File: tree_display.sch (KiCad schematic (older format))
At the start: 8 parts

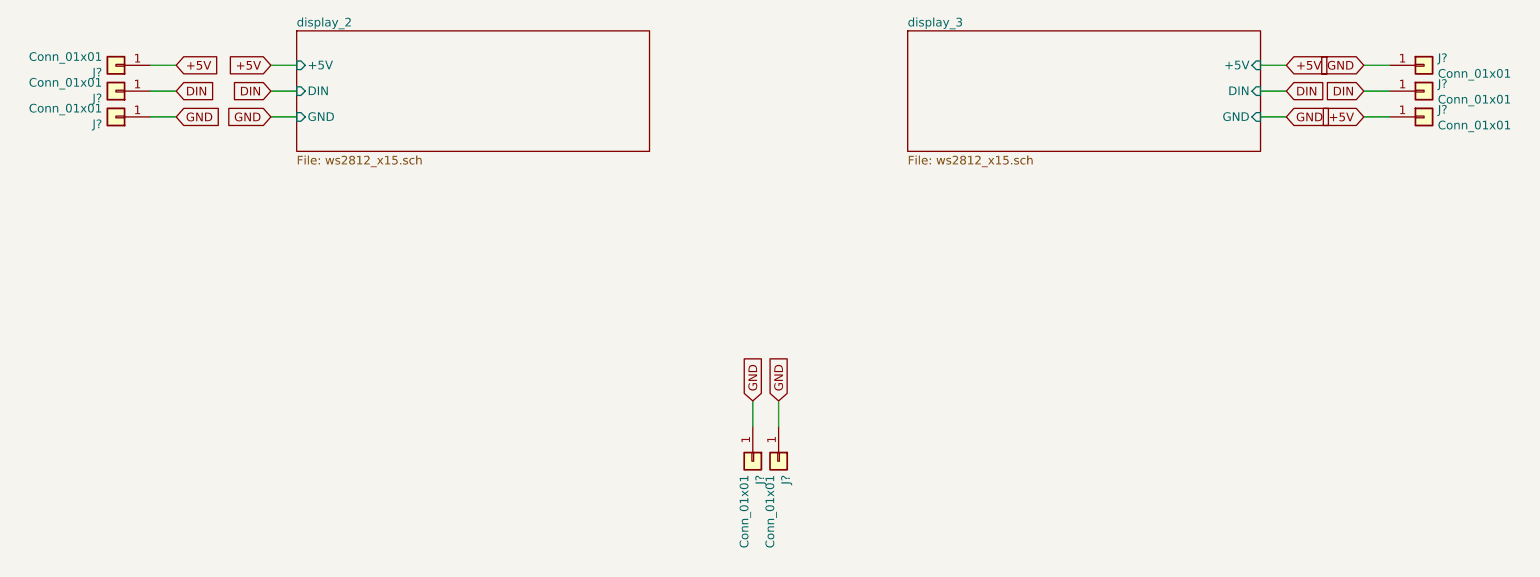
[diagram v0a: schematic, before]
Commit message: Update with changes to use attiny13a only
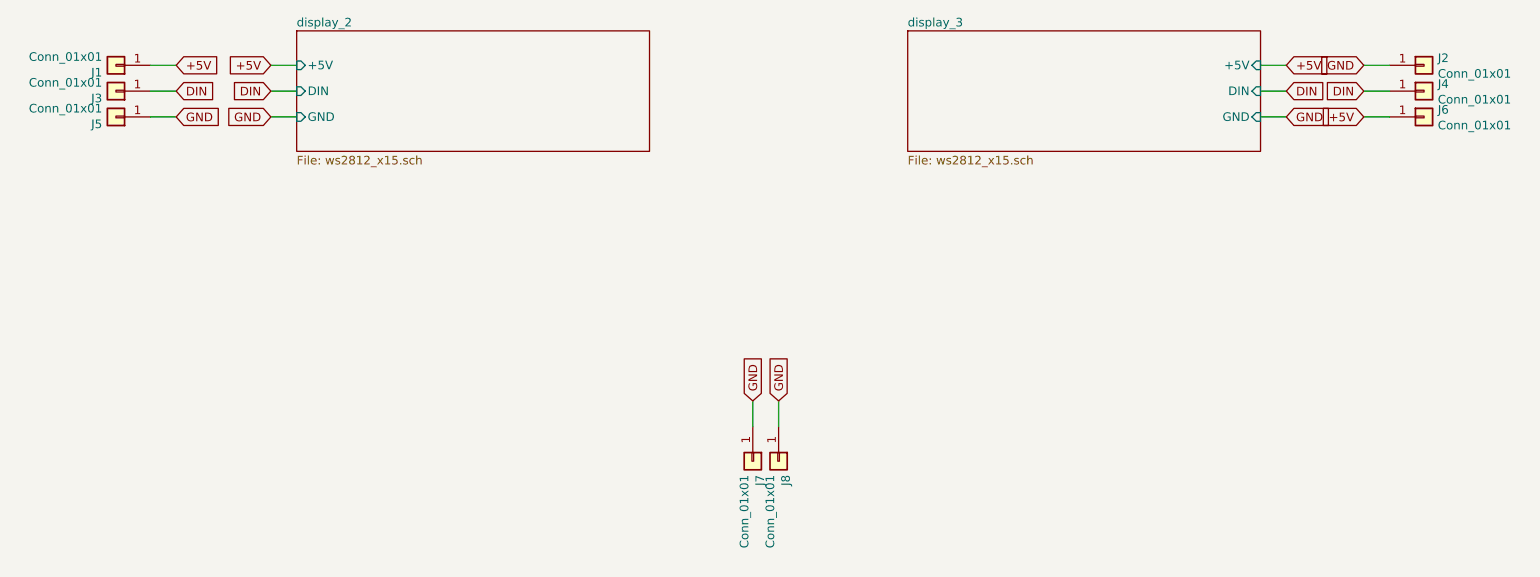
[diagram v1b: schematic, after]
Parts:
- gave numbers to parts that had none: 8
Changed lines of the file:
@@
 $EndDescr
 $Comp
-L Connector_Generic:Conn_01x01 J?
+L Connector_Generic:Conn_01x01 J6
 U 1 1 5FC428C8
 P 9750 3550
-F 0 "J?" H 9830 3592 50  0000 L CNN
+F 0 "J6" H 9830 3592 50  0000 L CNN
 F 1 "Conn_01x01" H 9830 3501 50  0000 L CNN
 F 2 "TestPoint:TestPoint_Pad_2.0x2.0mm" H 9750 3550 50  0001 C CNN
@@
 	9550 3550 9400 3550
 $Comp
-L Connector_Generic:Conn_01x01 J?
+L Connector_Generic:Conn_01x01 J4
 U 1 1 5FC43693
 P 9750 3400
-F 0 "J?" H 9830 3442 50  0000 L CNN
+F 0 "J4" H 9830 3442 50  0000 L CNN
 F 1 "Conn_01x01" H 9830 3351 50  0000 L CNN
 F 2 "TestPoint:TestPoint_Pad_2.0x2.0mm" H 9750 3400 50  0001 C CNN
@@
 	9550 3400 9400 3400
 $Comp
-L Connector_Generic:Conn_01x01 J?
+L Connector_Generic:Conn_01x01 J2
 U 1 1 5FC43C3D
 P 9750 3250
-F 0 "J?" H 9830 3292 50  0000 L CNN
+F 0 "J2" H 9830 3292 50  0000 L CNN
 F 1 "Conn_01x01" H 9830 3201 50  0000 L CNN
 F 2 "TestPoint:TestPoint_Pad_2.0x2.0mm" H 9750 3250 50  0001 C CNN
@@
 	9550 3250 9400 3250
 $Comp
-L Connector_Generic:Conn_01x01 J?
+L Connector_Generic:Conn_01x01 J1
 U 1 1 5FC48F56
 P 2150 3250
-F 0 "J?" H 2230 3292 50  0000 L CNN
+F 0 "J1" H 2230 3292 50  0000 L CNN
 F 1 "Conn_01x01" H 2230 3201 50  0000 L CNN
 F 2 "TestPoint:TestPoint_Pad_2.0x2.0mm" H 2150 3250 50  0001 C CNN
@@
 	2350 3250 2500 3250
 $Comp
-L Connector_Generic:Conn_01x01 J?
+L Connector_Generic:Conn_01x01 J3
 U 1 1 5FC48F5E
 P 2150 3400
-F 0 "J?" H 2230 3442 50  0000 L CNN
+F 0 "J3" H 2230 3442 50  0000 L CNN
 F 1 "Conn_01x01" H 2230 3351 50  0000 L CNN
 F 2 "TestPoint:TestPoint_Pad_2.0x2.0mm" H 2150 3400 50  0001 C CNN
@@
 	2350 3400 2500 3400
 $Comp
-L Connector_Generic:Conn_01x01 J?
+L Connector_Generic:Conn_01x01 J5
 U 1 1 5FC48F66
 P 2150 3550
-F 0 "J?" H 2230 3592 50  0000 L CNN
+F 0 "J5" H 2230 3592 50  0000 L CNN
 F 1 "Conn_01x01" H 2230 3501 50  0000 L CNN
 F 2 "TestPoint:TestPoint_Pad_2.0x2.0mm" H 2150 3550 50  0001 C CNN
@@
 GND
 $Comp
-L Connector_Generic:Conn_01x01 J?
+L Connector_Generic:Conn_01x01 J8
 U 1 1 5FC50D76
 P 6000 5550
-F 0 "J?" H 6080 5592 50  0000 L CNN
+F 0 "J8" H 6080 5592 50  0000 L CNN
 F 1 "Conn_01x01" H 6080 5501 50  0000 L CNN
 F 2 "TestPoint:TestPoint_Pad_2.0x2.0mm" H 6000 5550 50  0001 C CNN
@@
 	6000 5350 6000 5200
 $Comp
-L Connector_Generic:Conn_01x01 J?
+L Connector_Generic:Conn_01x01 J7
 U 1 1 5FC51DA3
 P 5850 5550
-F 0 "J?" H 5930 5592 50  0000 L CNN
+F 0 "J7" H 5930 5592 50  0000 L CNN
 F 1 "Conn_01x01" H 5930 5501 50  0000 L CNN
 F 2 "TestPoint:TestPoint_Pad_2.0x2.0mm" H 5850 5550 50  0001 C CNN
